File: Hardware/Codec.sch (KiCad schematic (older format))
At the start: 11 parts, among them U301 SGTL5000XNAA3

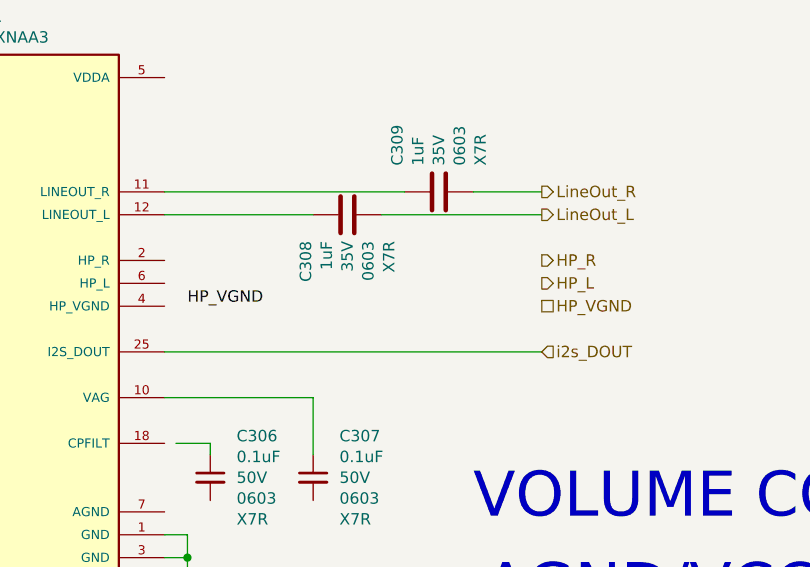
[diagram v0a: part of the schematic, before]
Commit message: Level shifting for DAC, some connectivity.
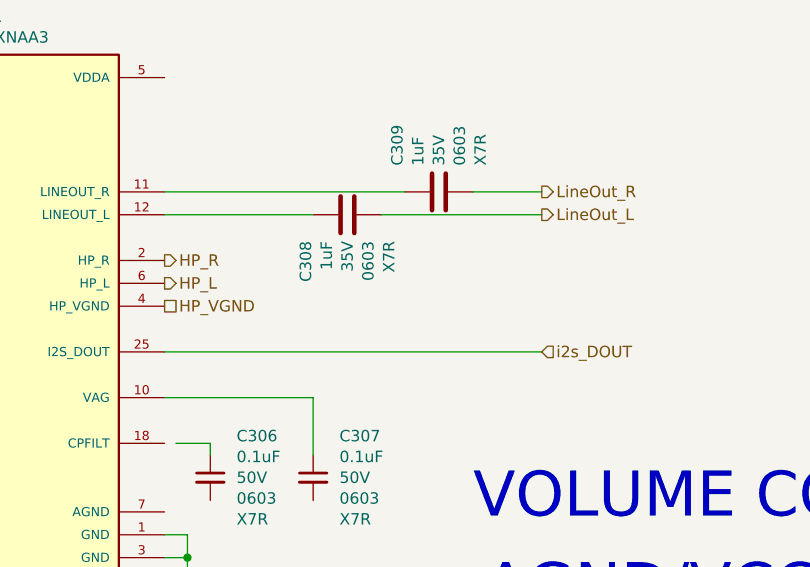
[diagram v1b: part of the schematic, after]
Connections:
- net HP_L: now also U301.6 (HP_L)
- net HP_R: now also U301.2 (HP_R)
- net HP_VGND: now also U301.4 (HP_VGND)
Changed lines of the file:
@@
 	0    1    1    0
 $EndComp
-Text Label 6150 3350 0    50   ~ 0
-HP_VGND
 Wire Wire Line
 	6150 4350 6050 4350
@@
 Text HLabel 1850 3150 0    50   Input ~ 0
 MIC_IN
-Text HLabel 7700 3150 2    50   Output ~ 0
+Text HLabel 6050 3150 2    50   Output ~ 0
 HP_R
-Text HLabel 7700 3250 2    50   Output ~ 0
+Text HLabel 6050 3250 2    50   Output ~ 0
 HP_L
-Text HLabel 7700 3350 2    50   UnSpc ~ 0
+Text HLabel 6050 3350 2    50   UnSpc ~ 0
 HP_VGND
 Wire Wire Line

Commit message: Connecting up SAO.
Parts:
- U301: DPN (none) -> SGTL5000XNAA3-ND; MPN (none) -> SGTL5000XNAA3
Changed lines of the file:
@@
 $Descr A4 11693 8268
 encoding utf-8
-Sheet 3 9
+Sheet 3 7
 Title ""
 Date ""
@@
 F 3 "" H 5250 3450 50  0001 L BNN
 F 4 "Freescale Semiconductor" H 5250 3450 50  0001 L BNN "MANUFACTURER"
+F 5 "SGTL5000XNAA3" H 5250 3450 50  0001 C CNN "MPN"
+F 6 "SGTL5000XNAA3-ND" H 5250 3450 50  0001 C CNN "DPN"
 	1    5250 3450
 	1    0    0    -1

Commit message: Commit berfore merge back with power fix.
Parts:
- added JP301: i2cAddr, Jumper:SolderJumper-2_P1.3mm_Bridged_RoundedPad1.0x1.5mm, symbol Jumper:SolderJumper_2_Bridged
- C306: value 0.1uF -> DNF; footprint Capacitor_SMD:C_0603_1608Metric -> Capacitor_SMD:C_0402_1005Metric; DPN 399-6856-1-ND -> (none); MPN C0603C104K5RACAUTO -> (none); Pkg 0603 -> (none); TCoff X7R -> (none); Tol 50V -> (none)
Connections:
- net +3V3: now also U301.5 (VDDA)
- net GND: now also C306.2, C307.2, U301.32 (CTRL_MODE), U301.7 (AGND), JP301.2 (B)
- net at U301.18 (CPFILT): now also C306.1
- net at U301.31 (CTRL_ADR0_CS): now also JP301.1 (A)
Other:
- note added: "Do not connect HP_VGND to system ground, even\nwhen unused. This is a virtual ground (DC voltage) that\nshould never connect to an actual “0 Volt ground”. Use\nthe widest, shortest trace possible for the HP_VGND.\n"
- note added: "The CPFILT cap value is 0.1uF. If both VDDIO and\nVDDA are <= 3.0 V, the CPFILT pin must be connected \nto a 0.1 uF cap to GND. If either is > 3.0 V, the CPFILT cap MUST NOT be placed."
- note added: "The PAD must be soldered to ground.\nStar the ground pins of the chip, VAG ground, and all\nanalog inputs/outputs to a single point, then to the\nground plane.\n"
- note removed: "VOLUME CONTROL??"
- moved on the sheet: C306
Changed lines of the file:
@@
 L Device:C_Small C?
 U 1 1 61383D31
-P 6250 4100
+P 6150 4100
 AR Path="/611E335F/61383D31" Ref="C?"  Part="1"
 AR Path="/611E3218/611E32E1/61383D31" Ref="C306"  Part="1"
-F 0 "C306" H 6365 4282 50  0000 L CNN
-F 1 "0.1uF" H 6365 4191 50  0000 L CNN
-F 2 "Capacitor_SMD:C_0603_1608Metric" H 6288 3950 50  0001 C CNN
-F 3 "~" H 6250 4100 50  0001 C CNN
-F 4 "C0603C104K5RACAUTO" H 6250 4100 50  0001 C CNN "MPN"
-F 5 "399-6856-1-ND" H 6250 4100 50  0001 C CNN "DPN"
-F 6 "50V" H 6365 4100 50  0000 L CNN "Tol"
-F 7 "0603" H 6365 4009 50  0000 L CNN "Pkg"
-F 8 "X7R" H 6365 3918 50  0000 L CNN "TCoff"
-	1    6250 4100
+F 0 "C306" H 6265 4282 50  0000 L CNN
+F 1 "DNF" H 6265 4191 50  0000 L CNN
+F 2 "Capacitor_SMD:C_0402_1005Metric" H 6188 3950 50  0001 C CNN
+F 3 "~" H 6150 4100 50  0001 C CNN
+F 4 "" H 6150 4100 50  0001 C CNN "MPN"
+F 5 "" H 6150 4100 50  0001 C CNN "DPN"
+F 6 "" H 6265 4100 50  0000 L CNN "Tol"
+F 7 "" H 6265 4009 50  0000 L CNN "Pkg"
+F 8 "" H 6265 3918 50  0000 L CNN "TCoff"
+	1    6150 4100
 	1    0    0    -1
 $EndComp
@@
 	6700 3750 6700 4000
 Wire Wire Line
-	6100 3950 6250 3950
-Wire Wire Line
-	6250 3950 6250 4000
+	6150 3950 6150 4000
 Text HLabel 1850 3150 0    50   Input ~ 0
 MIC_IN
@@
 	6150 4350 6150 4450
 Connection ~ 6150 4450
-Text Notes 7400 4300 0    197  ~ 0
-VOLUME CONTROL??
 Wire Wire Line
 	4450 2350 4350 2350
@@
 Text Notes 7450 4700 0    197  ~ 0
 AGND/VCCA FILTERS?
+Wire Wire Line
+	6050 4250 6150 4250
+Wire Wire Line
+	6150 4250 6150 4350
+Connection ~ 6150 4350
+$Comp
+L power:GND #PWR?
+U 1 1 616A5FE3
+P 4350 4600
+AR Path="/611E3335/616A5FE3" Ref="#PWR?"  Part="1"
+AR Path="/611E3218/611E32E1/616A5FE3" Ref="#PWR0179"  Part="1"
+F 0 "#PWR0179" H 4350 4350 50  0001 C CNN
+F 1 "GND" H 4355 4427 50  0000 C CNN
+F 2 "" H 4350 4600 50  0001 C CNN
+F 3 "" H 4350 4600 50  0001 C CNN
+	1    4350 4600
+	-1   0    0    -1
+$EndComp
+Wire Wire Line
+	4450 4250 4350 4250
+Wire Wire Line
+	4350 4250 4350 4600
+$Comp
+L Jumper:SolderJumper_2_Bridged JP301
+U 1 1 616A9E90
+P 3850 4450
+F 0 "JP301" V 3804 4518 50  0000 L CNN
+F 1 "i2cAddr" V 3850 4100 50  0000 L CNN
+F 2 "Jumper:SolderJumper-2_P1.3mm_Bridged_RoundedPad1.0x1.5mm" H 3850 4450 50  0001 C CNN
+F 3 "~" H 3850 4450 50  0001 C CNN
+	1    3850 4450
+	0    1    1    0
+$EndComp
+Wire Wire Line
+	3850 4150 3850 4300
+Wire Wire Line
+	3850 4150 4450 4150
+$Comp
+L power:GND #PWR?
+U 1 1 616AB03B
+P 3850 4600
+AR Path="/611E3335/616AB03B" Ref="#PWR?"  Part="1"
+AR Path="/611E3218/611E32E1/616AB03B" Ref="#PWR0180"  Part="1"
+F 0 "#PWR0180" H 3850 4350 50  0001 C CNN
+F 1 "GND" H 3855 4427 50  0000 C CNN
+F 2 "" H 3850 4600 50  0001 C CNN
+F 3 "" H 3850 4600 50  0001 C CNN
+	1    3850 4600
+	-1   0    0    -1
+$EndComp
+$Comp
+L power:+3V3 #PWR?
+U 1 1 616AD8A4
+P 6100 1850
+AR Path="/6123BB15/616AD8A4" Ref="#PWR?"  Part="1"
+AR Path="/611E335F/616AD8A4" Ref="#PWR?"  Part="1"
+AR Path="/611E3218/611E32E1/616AD8A4" Ref="#PWR0181"  Part="1"
+F 0 "#PWR0181" H 6100 1700 50  0001 C CNN
+F 1 "+3V3" H 6115 2023 50  0000 C CNN
+F 2 "" H 6100 1850 50  0001 C CNN
+F 3 "" H 6100 1850 50  0001 C CNN
+	1    6100 1850
+	1    0    0    -1
+$EndComp
+Wire Wire Line
+	6100 1850 6100 2350
+Wire Wire Line
+	6100 2350 6050 2350
+Wire Wire Line
+	6050 3950 6150 3950
+Text Notes 8000 1550 0    50   ~ 0
+The CPFILT cap value is 0.1uF. If both VDDIO and\nVDDA are <= 3.0 V, the CPFILT pin must be connected \nto a 0.1 uF cap to GND. If either is > 3.0 V, the CPFILT cap MUST NOT be placed.
+Wire Wire Line
+	6150 4200 6150 4250
+Connection ~ 6150 4250
+Text Notes 7500 5350 0    50   ~ 0
+The PAD must be soldered to ground.\nStar the ground pins of the chip, VAG ground, and all\nanalog inputs/outputs to a single point, then to the\nground plane.\n
+$Comp
+L power:GND #PWR?
+U 1 1 616B7426
+P 6700 4600
+AR Path="/611E3335/616B7426" Ref="#PWR?"  Part="1"
+AR Path="/611E3218/611E32E1/616B7426" Ref="#PWR0182"  Part="1"
+F 0 "#PWR0182" H 6700 4350 50  0001 C CNN
+F 1 "GND" H 6705 4427 50  0000 C CNN
+F 2 "" H 6700 4600 50  0001 C CNN
+F 3 "" H 6700 4600 50  0001 C CNN
+	1    6700 4600
+	-1   0    0    -1
+$EndComp
+Wire Wire Line
+	6700 4200 6700 4600
+Text Notes 8600 3350 0    50   ~ 0
+ Do not connect HP_VGND to system ground, even\nwhen unused. This is a virtual ground (DC voltage) that\nshould never connect to an actual “0 Volt ground”. Use\nthe widest, shortest trace possible for the HP_VGND.\n
 $EndSCHEMATC

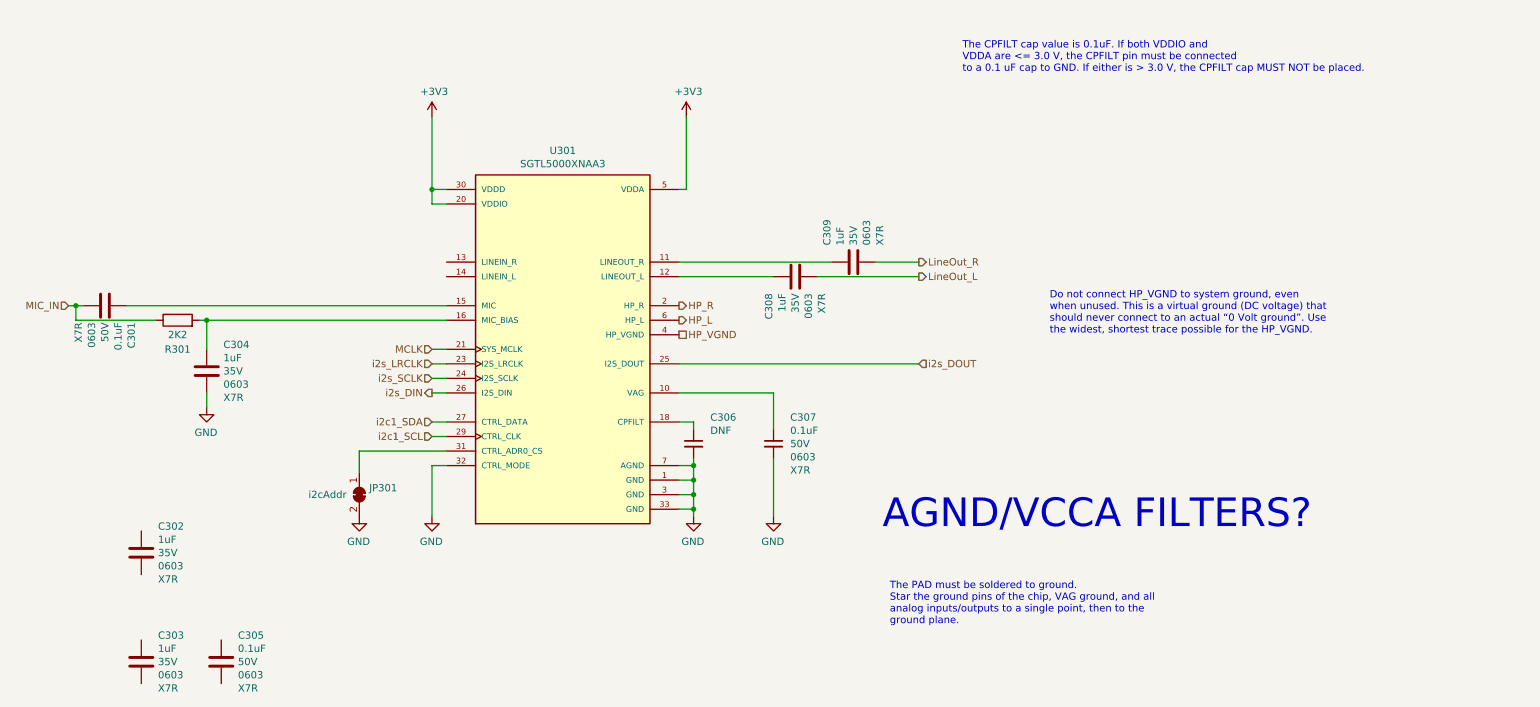
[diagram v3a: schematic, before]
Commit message: Fixing up some BoM repetition.
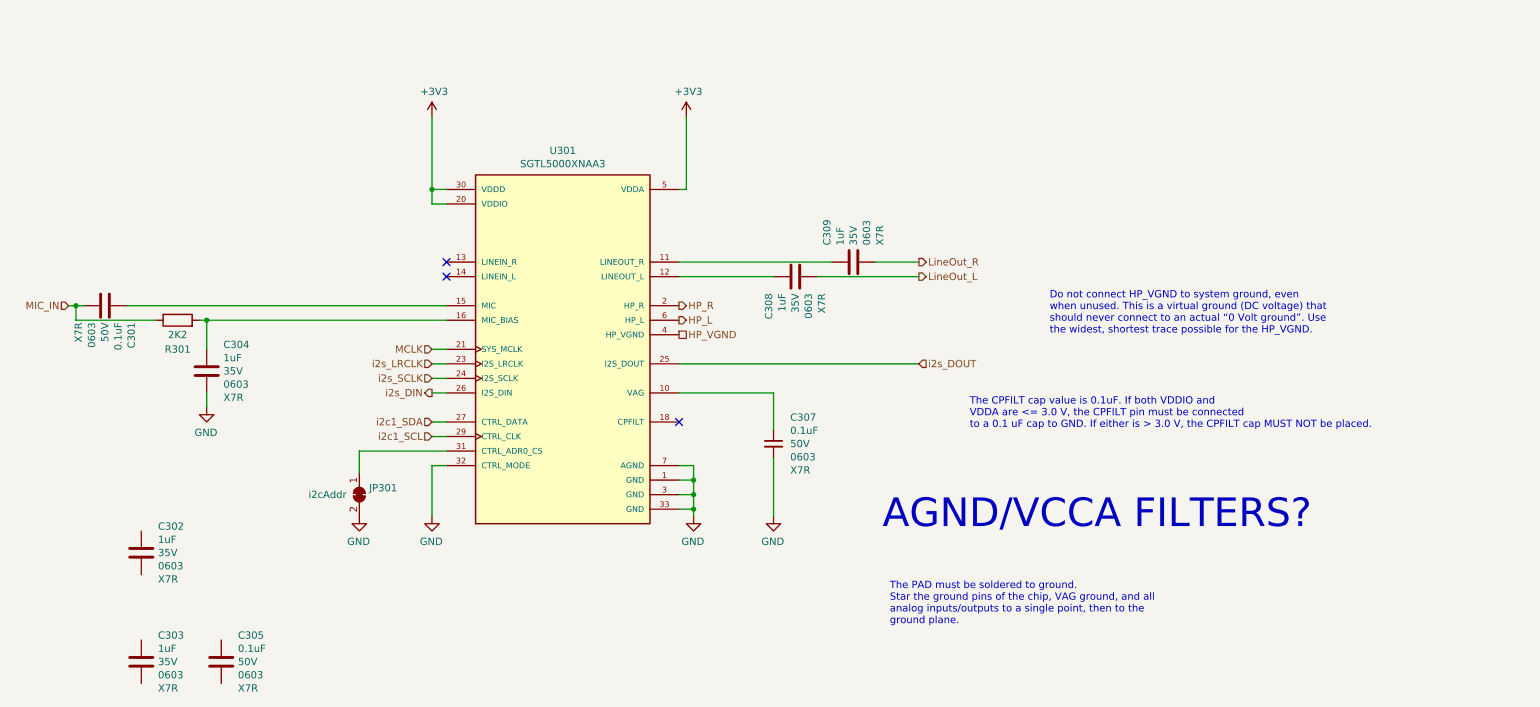
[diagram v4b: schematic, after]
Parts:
- removed C306: DNF, Capacitor_SMD:C_0402_1005Metric, symbol Device:C_Small
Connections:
- no-connect marks 0 -> 3
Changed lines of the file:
@@
 Wire Wire Line
 	6150 4350 6050 4350
-$Comp
-L Device:C_Small C?
-U 1 1 61383D31
-P 6150 4100
-AR Path="/611E335F/61383D31" Ref="C?"  Part="1"
-AR Path="/611E3218/611E32E1/61383D31" Ref="C306"  Part="1"
-F 0 "C306" H 6265 4282 50  0000 L CNN
-F 1 "DNF" H 6265 4191 50  0000 L CNN
-F 2 "Capacitor_SMD:C_0402_1005Metric" H 6188 3950 50  0001 C CNN
-F 3 "~" H 6150 4100 50  0001 C CNN
-F 4 "" H 6150 4100 50  0001 C CNN "MPN"
-F 5 "" H 6150 4100 50  0001 C CNN "DPN"
-F 6 "" H 6265 4100 50  0000 L CNN "Tol"
-F 7 "" H 6265 4009 50  0000 L CNN "Pkg"
-F 8 "" H 6265 3918 50  0000 L CNN "TCoff"
-	1    6150 4100
-	1    0    0    -1
-$EndComp
 Wire Wire Line
 	4350 3950 4450 3950
@@
 Wire Wire Line
 	6700 3750 6700 4000
-Wire Wire Line
-	6150 3950 6150 4000
 Text HLabel 1850 3150 0    50   Input ~ 0
 MIC_IN
@@
 Wire Wire Line
 	6100 2350 6050 2350
-Wire Wire Line
-	6050 3950 6150 3950
-Text Notes 8000 1550 0    50   ~ 0
+Text Notes 8050 4000 0    50   ~ 0
 The CPFILT cap value is 0.1uF. If both VDDIO and\nVDDA are <= 3.0 V, the CPFILT pin must be connected \nto a 0.1 uF cap to GND. If either is > 3.0 V, the CPFILT cap MUST NOT be placed.
-Wire Wire Line
-	6150 4200 6150 4250
-Connection ~ 6150 4250
 Text Notes 7500 5350 0    50   ~ 0
 The PAD must be soldered to ground.\nStar the ground pins of the chip, VAG ground, and all\nanalog inputs/outputs to a single point, then to the\nground plane.\n
@@
 Text Notes 8600 3350 0    50   ~ 0
  Do not connect HP_VGND to system ground, even\nwhen unused. This is a virtual ground (DC voltage) that\nshould never connect to an actual “0 Volt ground”. Use\nthe widest, shortest trace possible for the HP_VGND.\n
+NoConn ~ 6050 3950
+NoConn ~ 4450 2850
+NoConn ~ 4450 2950
 $EndSCHEMATC

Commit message: Most placements, testpoints and spare points added. Looking good.
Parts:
- JP301: footprint Jumper:SolderJumper-2_P1.3mm_Bridged_RoundedPad1.0x1.5mm -> OHMC2022:SolderJumper-2_P1.3mm_Bridged_RoundedPad1.0x1.5mm
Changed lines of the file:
@@
 F 0 "JP301" V 3804 4518 50  0000 L CNN
 F 1 "i2cAddr" V 3850 4100 50  0000 L CNN
-F 2 "Jumper:SolderJumper-2_P1.3mm_Bridged_RoundedPad1.0x1.5mm" H 3850 4450 50  0001 C CNN
+F 2 "OHMC2022:SolderJumper-2_P1.3mm_Bridged_RoundedPad1.0x1.5mm" H 3850 4450 50  0001 C CNN
 F 3 "~" H 3850 4450 50  0001 C CNN
 	1    3850 4450
